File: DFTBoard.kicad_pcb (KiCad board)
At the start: 8 copper layers, 276 parts, among them CON1 AVR-JTAG-10, CON2 AVR-JTAG-10, IC1 WM8758B, IC2 IS31FL3199, IC3 CyUSB30xx-BZX, J1 JACK_TRS_5PINS, J2 JACK_TRS_5PINS, J3 JACK_TRS_5PINS, J4 JACK_TRS_5PINS, J5 GSB3211311WEU, J6 48258-0001, J7 MICRO_HDMI, Q1 IRLML2502, Q2 IRLML2502, Q3 IRLML2502, Q4 IRLML2502, Q5 IRLML2502, Q6 IRLML2502, SW1 SW_IL, U1 xc7a50tftg256, U10 NC7WZ07P6X, U11 NC7SZ125M5X, U12 GTL2002, U13 ADP198ACPZ-R7, U2 24FC128, U3 N25Q128A, U4 SC189 - 3.3V, U5 SC189 - 1.0V, U6 SC189 - 1.2V, U7 SC189 - 1.8V, U8 VL53L0X, U9 MAX3421, X1 KC5032A, Y1 19.2MHz, Y2 12MHz

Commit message: ran all FX3 BGA traces
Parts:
- added GT1: GNDTIE, DFTcustom:gndtie, F.Cu at (258.6, 129.8)
- added R94: 10k, Resistors_SMD:R_1206, F.Cu at (28.2, 37.7)
- C63: value 0.1uF -> .1uF
- C64: value 0.1uF -> 22uF
- C65: value .1uF -> .01uF; footprint Capacitors_SMD:C_0603 -> Capacitors_SMD:C_0402
- C66: value 22uF -> .1uF
- C67: value .01uF -> 0.1uF; footprint Capacitors_SMD:C_0402 -> Capacitors_SMD:C_0603
- C68: value .1uF -> 0.1uF
- R32, R73: value 100k -> 10k
- R33: value 49.9k -> 165
- R34, R43: value 50k -> 100k
- R35, R41: value 100k -> 49.9k
- R36: value 100k -> 50k
- R38, R39: value 49.9k -> 100k
- R42: value 50k -> 49.9k
- R44: value 20k -> 4.7k
- R46: value 4.7k -> 10k
- R47: value 10k -> 37.5
- R49: value 37.5 -> 50k
- R50: value 50k -> 6.04k
- R51: value 6.04k -> 200
- R52: value 200 -> 10k
- R54: value 10k -> 1k
- R55: value 1k -> 145
- R56: value 145 -> 1k
- R57: value 1k -> 90
- R58: value 90 -> 20k
- R59: value 20k -> 33; moved to B.Cu
- R61: value 33 -> 20k
- R62: value 20k -> 1k
- R64: value 1k -> 100k
- R65: value 100k -> 1k
- R66: value 1MEG -> 27k
- R67: value 1k -> 1MEG
- R68: value 27k -> 200k
- R69: value 200k -> 1k
- R70: value 1k -> 1.5k
- R72: value 1.5k -> 100k
- U3: value N25Q128A -> W25Q128FW; footprint SMD_Packages:SO-16-N -> SMD_Packages:SOIC-8-N
- moved FB2 166.0 mm to (253.2, 119.0), turned to 180 degrees
- moved C67 156.4 mm to (246.6, 126.4), turned to 180 degrees
- moved C68 150.1 mm to (249.6, 125.6), turned to 180 degrees
- moved DS1 143.0 mm to (231.8, 86.6), turned to 90 degrees
- moved CON1 130.0 mm to (111.3, 78.3)
- moved R59 109.9 mm to (259.1, 151.7), turned to 180 degrees
- moved R93 104.8 mm to (34.5, 36.6)
- moved CON2 18.5 mm to (102.2, 102.8)
- moved C64 11.0 mm to (257.9, 118.8)
- moved R61 10.0 mm to (249.3, 142.2), turned to 270 degrees
- moved C63 7.97 mm to (249.6, 119.0)
- moved IC1 7.39 mm to (82.2, 85.8)
- moved NCP1 7.21 mm to (253.9, 142.4)
- moved R60 3.64 mm to (259.1, 149.1)
- moved U9 1.73 mm to (246.5, 150.4)
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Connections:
- net Net-(C26-Pad1) renamed /Audio/MIC_IN_P
- net Net-(C26-Pad2) renamed /Audio/SFG
- net Net-(C28-Pad2) renamed /Audio/LINE_COM
- net Net-(C33-Pad1) renamed /Audio/HP_COM
- net Net-(C34-Pad1) renamed /Audio/VMID
- net Net-(C35-Pad1) renamed /Audio/MICBIAS
- net Net-(C36-Pad2) renamed /Audio/HPLOUT
- net Net-(C44-Pad1) renamed /LEDs/C_FILT
- net Net-(D1-Pad1) renamed /FPGA/Configuration/DONE_LED_D
- net Net-(D1-Pad2) renamed /FPGA/Configuration/DONE_LED_R
- net Net-(D2-Pad1) renamed /FPGA/Configuration/INIT_LED_D
- net Net-(D2-Pad2) renamed /FPGA/Configuration/INIT_LED_R
- net Net-(D3-Pad1) renamed /LEDs/LED_1R
- net Net-(D3-Pad2) renamed /LEDs/LED_1G
- net Net-(D3-Pad3) renamed /LEDs/LED_1B
- net Net-(D4-Pad1) renamed /LEDs/LED_3R
- net Net-(D4-Pad2) renamed /LEDs/LED_3G
- net Net-(D4-Pad3) renamed /LEDs/LED_3B
- net Net-(D5-Pad1) renamed /LEDs/LED_2R
- net Net-(D5-Pad2) renamed /LEDs/LED_2G
- net Net-(D5-Pad3) renamed /LEDs/LED_2B
- net Net-(D6-Pad1) renamed /SPIUSBBRIDGE/RED_LED_D
- net Net-(D7-Pad1) renamed /SPIUSBBRIDGE/BLUE_LED_D
- net Net-(DS1-Pad3) renamed /Cypress FX3/LCD_V0
- net Net-(IC1-Pad1) renamed /Audio/JACK_IN_P
- net Net-(IC1-Pad2) renamed /Audio/JACK_IN_N
- net Net-(IC1-Pad29) renamed /Audio/ROUT1
- net Net-(IC1-Pad30) renamed /Audio/LOUT1
- net Net-(IC3-PadG4) renamed /Cypress FX3/FX_P0
- net Net-(L1-Pad1) renamed /Power/3V3TOLX
- net Net-(L2-Pad1) renamed /Power/1V0TOLX
- net Net-(L3-Pad1) renamed /Power/1V2TOLX
- net Net-(L4-Pad1) renamed /Power/1V8TOLX
- net Net-(Q1-Pad1) renamed /FPGA/Configuration/DONE_LED_G
- net Net-(Q2-Pad1) renamed /FPGA/Configuration/INIT_LED_G
- net Net-(Q4-Pad1) renamed /Cypress FX3/LCD_LED_PWM
- C1 pad 2: AGND -> GND
- C10 pad 2: AGND -> GND
- C100 pad 2: AGND -> GND
- C101 pad 1: AGND -> GND
- C102 pad 1: AGND -> GND
- C103 pad 2: AGND -> GND
- C104 pad 2: AGND -> GND
- C105 pad 2: AGND -> GND
- C106 pad 1: Net-(C106-Pad1) -> /HDMI/BUF_REF
- C106 pad 2: AGND -> GND
- C107 pad 1: AGND -> GND
- C107 pad 2: /HDMI/HDMI_SHD -> HDMI_SHD
- C108 pad 2: AGND -> GND
- C109 pad 2: AGND -> GND
- C11 pad 2: AGND -> GND
- C110 pad 2: AGND -> GND
- C111 pad 2: AGND -> GND
- C112 pad 2: AGND -> GND
- C113 pad 2: AGND -> GND
- C114 pad 2: AGND -> GND
- C115 pad 2: AGND -> GND
- C116 pad 2: AGND -> GND
- C117 pad 2: AGND -> GND
- C118 pad 2: AGND -> GND
- C119 pad 2: AGND -> GND
- C12 pad 2: AGND -> GND
- C120 pad 2: AGND -> GND
- C121 pad 2: AGND -> GND
- C122 pad 2: AGND -> GND
- C123 pad 2: AGND -> GND
- C124 pad 2: AGND -> GND
- C125 pad 2: AGND -> GND
- C13 pad 2: AGND -> GND
- C14 pad 2: AGND -> GND
- C15 pad 2: AGND -> GND
- C16 pad 2: AGND -> GND
- C17 pad 2: AGND -> GND
- C18 pad 2: AGND -> GND
- C19 pad 2: AGND -> GND
- C2 pad 2: AGND -> GND
- C20 pad 2: AGND -> GND
- C21 pad 2: AGND -> GND
- C22 pad 2: AGND -> GND
- C23 pad 2: AGND -> GND
- C24 pad 2: AGND -> GND
- C25 pad 2: AGND -> GND
- C27 pad 2: AGND -> GND
- C28 pad 1: AGND -> GNDA
- C29 pad 2: AGND -> GND
- C3 pad 2: AGND -> GND
- C30 pad 2: AGND -> GND
- C31 pad 2: AGND -> GND
- C32 pad 2: AGND -> GND
- C33 pad 2: AGND -> GNDA
- C34 pad 2: AGND -> GNDA
- C35 pad 2: AGND -> GNDA
- C38 pad 2: AGND -> GND
- C39 pad 2: AGND -> GND
- C4 pad 2: AGND -> GND
- C40 pad 2: AGND -> GND
- C42 pad 2: AGND -> GND
- C43 pad 2: AGND -> GND
- C44 pad 2: AGND -> GND
- C45 pad 2: AGND -> GND
- C46 pad 2: AGND -> GND
- C47 pad 2: AGND -> GND
- C48 pad 2: AGND -> GND
- C49 pad 2: AGND -> GND
- C5 pad 2: AGND -> GND
- C50 pad 2: AGND -> GND
- C51 pad 2: AGND -> GND
- C52 pad 2: AGND -> GND
- C53 pad 2: AGND -> GND
- C54 pad 2: AGND -> GND
- C55 pad 2: AGND -> GND
- C56 pad 2: AGND -> GND
- C57 pad 2: AGND -> GND
- C58 pad 2: AGND -> GND
- C59 pad 2: AGND -> GND
- C6 pad 2: AGND -> GND
- C60 pad 2: AGND -> GND
- C61 pad 2: AGND -> GND
- C62 pad 2: AGND -> GND
- C63 pad 1: SSTX_N -> +1.2V
- C63 pad 2: /Cypress FX3/SSTXAC_N -> GND
- C64 pad 1: SSTX_P -> /Cypress FX3/U3RXVDDQ
- C64 pad 2: /Cypress FX3/SSTXAC_P -> GND
- C65 pad 1: +1.2V -> +1.8V
- C65 pad 2: AGND -> GND
- C66 pad 1: /Cypress FX3/U3RXVDDQ -> +1.2V
- C66 pad 2: AGND -> GND
- C67 pad 1: +1.8V -> SSTX_N
- C67 pad 2: AGND -> /Cypress FX3/SSTXAC_N
- C68 pad 1: +1.2V -> SSTX_P
- C68 pad 2: AGND -> /Cypress FX3/SSTXAC_P
- C69 pad 2: AGND -> GND
- C7 pad 2: AGND -> GND
- C70 pad 2: AGND -> GND
- C71 pad 2: AGND -> GND
- C72 pad 2: AGND -> GND
- C73 pad 2: AGND -> GND
- C74 pad 2: AGND -> GND
- C75 pad 2: AGND -> GND
- C76 pad 2: AGND -> GND
- C77 pad 2: AGND -> GND
- C78 pad 2: AGND -> GND
- C79 pad 2: AGND -> GND
- C8 pad 2: AGND -> GND
- C80 pad 2: AGND -> GND
- C81 pad 2: AGND -> GND
- C82 pad 2: AGND -> GND
- C83 pad 2: AGND -> GND
- C84 pad 2: AGND -> GND
- C85 pad 2: AGND -> GND
- C86 pad 2: AGND -> GND
- C87 pad 2: AGND -> GND
- C88 pad 2: AGND -> GND
- C89 pad 2: AGND -> GND
- C9 pad 2: AGND -> GND
- C90 pad 2: AGND -> GND
- C91 pad 2: AGND -> GND
- C92 pad 2: AGND -> GND
- C93 pad 2: AGND -> GND
- C94 pad 2: AGND -> GND
- C95 pad 2: AGND -> GND
- C96 pad 2: AGND -> GND
- C97 pad 2: AGND -> GND
- C98 pad 2: AGND -> GND
- C99 pad 2: AGND -> GND
- CON1 pad 10: AGND -> GND
- CON1 pad 2: AGND -> GND
- CON2 pad 10: AGND -> GND
- CON2 pad 2: AGND -> GND
- D6 pad 2: Net-(D6-Pad2) -> /SPIUSBBRIDGE/RED_LED_R
- D7 pad 2: Net-(D7-Pad2) -> /SPIUSBBRIDGE/BLUE_LED_R
- DS1 pad 1: AGND -> GND
- DS1 pad 15: Net-(DS1-Pad15) -> /Cypress FX3/LCD_LED_P
- DS1 pad 5: AGND -> GND
- IC1 pad 12: AGND -> GND
- IC1 pad 15: Net-(IC1-Pad15) -> /Audio/CSB
- IC1 pad 18: AGND -> GND
- IC1 pad 24: AGND -> GNDA
- IC1 pad 28: AGND -> GNDA
- IC1 pad 33: AGND -> GND
- IC1 pad 5: AGND -> GNDA
- IC2 pad 15: Net-(IC2-Pad15) -> /LEDs/R_EXT
- IC2 pad 16: Net-(IC2-Pad16) -> GND
- IC2 pad 7: AGND -> GND
- IC3 pad A1: AGND -> GND
- IC3 pad A8: AGND -> GND
- IC3 pad B2: AGND -> GND
- IC3 pad B4: AGND -> GND
- IC3 pad B7: AGND -> GND
- IC3 pad B8: AGND -> GND
- IC3 pad B9: AGND -> GND
- IC3 pad D8: AGND -> GND
- IC3 pad E2: AGND -> GND
- IC3 pad E6: AGND -> GND
- IC3 pad G1: AGND -> GND
- IC3 pad G11: AGND -> GND
- IC3 pad H4: Net-(IC3-PadH4) -> /Cypress FX3/FX_P1
- IC3 pad K3: AGND -> GND
- IC3 pad K4: AGND -> GND
- IC3 pad L1: AGND -> GND
- IC3 pad L11: AGND -> GND
- IC3 pad L2: AGND -> GND
- IC3 pad L3: AGND -> GND
- IC3 pad L6: AGND -> GND
- J1 pad S: AGND -> GNDA
- J1 pad TB: Net-(J1-PadTB) -> /Audio/INSWITCH
- J2 pad RB: Net-(J2-PadRB) -> /Audio/HPSWITCH
- J2 pad S: AGND -> GNDA
- J3 pad R: AGND -> GNDA
- J3 pad RB: AGND -> GNDA
- J3 pad S: AGND -> GNDA
- J3 pad TB: Net-(J3-PadTB) -> /Audio/RSWITCH
- J4 pad R: AGND -> GNDA
- J4 pad RB: AGND -> GNDA
- J4 pad S: AGND -> GNDA
- J4 pad TB: Net-(J4-PadTB) -> /Audio/LSWITCH
- J5 pad 4: AGND -> GNDPWR
- J5 pad 7: AGND -> GNDPWR
- J6 pad 4: AGND -> GND
- J6 pad P1: AGND -> GND
- J6 pad P2: AGND -> GND
- J7 pad 1: Net-(J7-Pad1) -> /HDMI/HDMI_DETECT_PIN
- J7 pad 10: AGND -> GND
- J7 pad 13: AGND -> GND
- J7 pad 16: AGND -> GND
- J7 pad 17: Net-(J7-Pad17) -> HDMI_SCL_B
- J7 pad 18: Net-(J7-Pad18) -> HDMI_SDA_B
- J7 pad 4: AGND -> GND
- J7 pad 7: AGND -> GND
- J7 pad SHD: /HDMI/HDMI_SHD -> HDMI_SHD
- JP1 pad 2: Net-(IC3-PadH4) -> /Cypress FX3/FX_P1
- MIC1 pad 2: AGND -> GNDA
- MIC1 pad 3: AGND -> GNDA
- NCP1 pad 2: AGND -> GND
- NCP1 pad 3: AGND -> GND
- Q1 pad 2: AGND -> GND
- Q2 pad 2: AGND -> GND
- Q3 pad 2: AGND -> GND
- Q4 pad 2: AGND -> GND
- Q5 pad 1: Net-(Q5-Pad1) -> /SPIUSBBRIDGE/RED_LED_G
- Q5 pad 2: AGND -> GND
- Q6 pad 1: Net-(Q6-Pad1) -> /SPIUSBBRIDGE/BLUE_LED_G
- Q6 pad 2: AGND -> GND
- R32 pad 2: Net-(J1-PadTB) -> TEMPO_SW
- R33 pad 1: JD_IN -> +5V
- R33 pad 2: Net-(J1-PadTB) -> /FPGA/GPIF II/TEMPO_LED_R
- R34 pad 2: Net-(IC1-Pad15) -> /Audio/INSWITCH
- R35 pad 1: Net-(J3-PadTB) -> JD_IN
- R35 pad 2: +3V3 -> /Audio/INSWITCH
- R36 pad 1: Net-(J4-PadTB) -> +1.8V
- R36 pad 2: +3V3 -> /Audio/CSB
- R37 pad 1: Net-(J2-PadRB) -> /Audio/RSWITCH
- R38 pad 1: JD_ROUT -> /Audio/LSWITCH
- R38 pad 2: Net-(J3-PadTB) -> +3V3
- R39 pad 1: JD_LOUT -> /Audio/HPSWITCH
- R39 pad 2: Net-(J4-PadTB) -> +3V3
- R40 pad 1: JD_HOUT -> JD_ROUT
- R40 pad 2: Net-(J2-PadRB) -> /Audio/RSWITCH
- R41 pad 1: Net-(IC2-Pad15) -> JD_LOUT
- R41 pad 2: AGND -> /Audio/LSWITCH
- R42 pad 1: Net-(IC2-Pad16) -> JD_HOUT
- R42 pad 2: AGND -> /Audio/HPSWITCH
- R43 pad 1: Net-(R43-Pad1) -> /LEDs/R_EXT
- R43 pad 2: +1.8V -> GND
- R44 pad 1: +1.8V -> I2C_SCLK
- R44 pad 2: Net-(R44-Pad2) -> +1.8V
- R45 pad 1: I2C_SCLK -> I2C_SDIN
- R46 pad 1: I2C_SDIN -> +1.8V
- R46 pad 2: +1.8V -> /Cypress FX3/FX_P1
- R47 pad 1: +1.8V -> /Cypress FX3/LCD_LED_P
- R47 pad 2: Net-(IC3-PadH4) -> +5V
- R49 pad 1: Net-(DS1-Pad15) -> CVDDQ
- R49 pad 2: +5V -> /Cypress FX3/nRESET
- R50 pad 1: CVDDQ -> /Cypress FX3/RUSB2
- R50 pad 2: /Cypress FX3/nRESET -> GND
- R51 pad 1: /Cypress FX3/RUSB2 -> /Cypress FX3/RUSB3
- R51 pad 2: AGND -> GND
- R52 pad 1: /Cypress FX3/RUSB3 -> +1.8V
- R52 pad 2: AGND -> RF_SD
- R53 pad 2: RF_SD -> RF_IRQ
- R54 pad 1: +1.8V -> /SPIUSBBRIDGE/RED_LED_G
- R54 pad 2: RF_IRQ -> /SPIUSBBRIDGE/GPOUT5_RED_LED
- R55 pad 1: Net-(Q5-Pad1) -> /SPIUSBBRIDGE/RED_LED_R
- R55 pad 2: Net-(R55-Pad2) -> +5V
- R56 pad 1: Net-(D6-Pad2) -> /SPIUSBBRIDGE/BLUE_LED_G
- R56 pad 2: +5V -> /SPIUSBBRIDGE/GPOUT6_BLUE_LED
- R57 pad 1: Net-(Q6-Pad1) -> /SPIUSBBRIDGE/BLUE_LED_R
- R57 pad 2: Net-(R57-Pad2) -> +5V
- R58 pad 1: Net-(D7-Pad2) -> +1.8V
- R58 pad 2: +5V -> /SPIUSBBRIDGE/RES
- R59 pad 1: +1.8V -> SPIUSB_D_P
- R59 pad 2: Net-(R59-Pad2) -> /SPIUSBBRIDGE/SPIUSB_DT_P
- R60 pad 1: SPIUSB_D_P -> SPIUSB_D_N
- R60 pad 2: /SPIUSBBRIDGE/SPIUSB_DT_P -> /SPIUSBBRIDGE/SPIUSB_DT_N
- R61 pad 1: SPIUSB_D_N -> +5V
- R61 pad 2: /SPIUSBBRIDGE/SPIUSB_DT_N -> USB_FAULT
- R62 pad 1: +5V -> +3V3
- R62 pad 2: USB_FAULT -> HDMI_SCL
- R63 pad 2: HDMI_SCL -> HDMI_SDA
- R64 pad 1: +3V3 -> /HDMI/HDMI_DETECT_PIN
- R64 pad 2: HDMI_SDA -> GND
- R65 pad 1: Net-(J7-Pad1) -> /HDMI/HDMI_DETECT_B2
- R65 pad 2: AGND -> /HDMI/HDMI_DETECT_PIN
- R66 pad 1: AGND -> (no net)
- R66 pad 2: /HDMI/HDMI_SHD -> +3V3
- R67 pad 1: Net-(R67-Pad1) -> GND
- R67 pad 2: Net-(J7-Pad1) -> HDMI_SHD
- R68 pad 1: (no net) -> HDMI_5V0
- R68 pad 2: +3V3 -> /HDMI/BUF_REF
- R69 pad 1: HDMI_5V0 -> HDMI_DETECT
- R69 pad 2: Net-(C106-Pad1) -> /HDMI/HDMI_DETECT_B1
- R70 pad 1: HDMI_DETECT -> HDMI_5V0
- R70 pad 2: Net-(R70-Pad2) -> HDMI_SCL_B
- R71 pad 2: Net-(J7-Pad17) -> HDMI_SDA_B
- R72 pad 1: HDMI_5V0 -> HDMI_DETECT
- R72 pad 2: Net-(J7-Pad18) -> GND
- R73 pad 1: HDMI_DETECT -> +1.8V
- R73 pad 2: AGND -> ENCC0_SW
- R74 pad 2: ENCC0_SW -> ENCC2_SW
- R75 pad 2: ENCC2_SW -> Net-(R75-Pad2)
- R79 pad 1: +1.8V -> ENCC0_Q0
- R79 pad 2: Net-(R79-Pad2) -> Net-(R75-Pad2)
- R80 pad 1: ENCC0_Q0 -> ENCC0_Q1
- R80 pad 2: Net-(R76-Pad2) -> Net-(R77-Pad2)
- R81 pad 1: ENCC0_Q1 -> ENCC2_Q0
- R81 pad 2: Net-(R78-Pad2) -> Net-(R76-Pad2)
- R82 pad 1: ENCC2_Q0 -> ENCC2_Q1
- R82 pad 2: Net-(R77-Pad2) -> Net-(R78-Pad2)
- R83 pad 1: ENCC2_Q1 -> +1.8V
- R83 pad 2: Net-(R79-Pad2) -> ENCC1_SW
- R84 pad 1: +1.8V -> +3V3
- R84 pad 2: ENCC1_SW -> ENCC3_SW
- R85 pad 1: +3V3 -> +1.8V
- R85 pad 2: ENCC3_SW -> Net-(R85-Pad2)
- R86 pad 1: +1.8V -> +3V3
- R87 pad 1: +3V3 -> +1.8V
- R88 pad 1: +1.8V -> +3V3
- R89 pad 1: +3V3 -> ENCC1_Q0
- R89 pad 2: Net-(R89-Pad2) -> Net-(R85-Pad2)
- R90 pad 1: ENCC1_Q0 -> ENCC1_Q1
- R90 pad 2: Net-(R86-Pad2) -> Net-(R87-Pad2)
- R91 pad 1: ENCC1_Q1 -> ENCC3_Q0
- R91 pad 2: Net-(R88-Pad2) -> Net-(R86-Pad2)
- R92 pad 1: ENCC3_Q0 -> ENCC3_Q1
- R92 pad 2: Net-(R87-Pad2) -> Net-(R88-Pad2)
- R93 pad 1: ENCC3_Q1 -> +1.8V
- R93 pad 2: Net-(R89-Pad2) -> Net-(R93-Pad2)
- ROT1 pad A: Net-(R76-Pad2) -> Net-(R75-Pad2)
- ROT1 pad B: Net-(R78-Pad2) -> Net-(R77-Pad2)
- ROT1 pad C: AGND -> GND
- ROT1 pad S2: AGND -> GND
- ROT2 pad A: Net-(R77-Pad2) -> Net-(R76-Pad2)
- ROT2 pad B: Net-(R79-Pad2) -> Net-(R78-Pad2)
- ROT2 pad C: AGND -> GND
- ROT2 pad S2: AGND -> GND
- ROT3 pad A: Net-(R86-Pad2) -> Net-(R85-Pad2)
- ROT3 pad B: Net-(R88-Pad2) -> Net-(R87-Pad2)
- ROT3 pad C: AGND -> GND
- ROT3 pad S2: AGND -> GND
- ROT4 pad A: Net-(R87-Pad2) -> Net-(R86-Pad2)
- ROT4 pad B: Net-(R89-Pad2) -> Net-(R88-Pad2)
- ROT4 pad C: AGND -> GND
- ROT4 pad S2: AGND -> GND
- RV1 pad 1: AGND -> GND
- SW1 pad 1: AGND -> GND
- SW1 pad 4: +5V -> /FPGA/GPIF II/TEMPO_LED_R
- U1 pad A1: AGND -> GND
- U1 pad A11: AGND -> GND
- U1 pad A16: AGND -> GND
- U1 pad B13: AGND -> GND
- U1 pad B8: AGND -> GND
- U1 pad C10: AGND -> GND
- U1 pad C15: AGND -> GND
- U1 pad C5: AGND -> GND
- U1 pad D12: AGND -> GND
- U1 pad D2: AGND -> GND
- U1 pad E14: AGND -> GND
- U1 pad E7: AGND -> GND
- U1 pad E9: AGND -> GND
- U1 pad F10: AGND -> GND
- U1 pad F16: AGND -> GND
- U1 pad F6: AGND -> GND
- U1 pad F8: AGND -> GND
- U1 pad G13: AGND -> GND
- U1 pad G3: AGND -> GND
- U1 pad G7: AGND -> GND
- U1 pad G9: AGND -> GND
- U1 pad H15: AGND -> GND
- U1 pad H6: AGND -> GND
- U1 pad H7: AGND -> GND
- U1 pad H8: AGND -> GND
- U1 pad J11: AGND -> GND
- U1 pad J12: AGND -> GND
- U1 pad J7: AGND -> GND
- U1 pad J8: AGND -> GND
- U1 pad J9: AGND -> GND
- U1 pad K14: AGND -> GND
- U1 pad K4: AGND -> GND
- U1 pad K6: AGND -> GND
- U1 pad K7: AGND -> GND
- U1 pad K8: AGND -> GND
- U1 pad L1: AGND -> GND
- U1 pad L11: AGND -> GND
- U1 pad M3: AGND -> GND
- U1 pad M8: AGND -> GND
- U1 pad N15: AGND -> GND
- U1 pad N5: AGND -> GND
- U1 pad P12: AGND -> GND
- U1 pad P2: AGND -> GND
- U1 pad R4: AGND -> GND
- U1 pad R9: AGND -> GND
- U1 pad T1: AGND -> GND
- U1 pad T16: AGND -> GND
- U1 pad T6: AGND -> GND
- U10 pad 1: Net-(J7-Pad1) -> /HDMI/HDMI_DETECT_PIN
- U10 pad 2: AGND -> GND
- U10 pad 6: Net-(R70-Pad2) -> /HDMI/HDMI_DETECT_B1
- U11 pad 3: AGND -> GND
- U11 pad 4: Net-(R67-Pad1) -> /HDMI/HDMI_DETECT_B2
- U12 pad 1: AGND -> GND
- U12 pad 5: Net-(J7-Pad18) -> HDMI_SDA_B
- U12 pad 6: Net-(J7-Pad17) -> HDMI_SCL_B
- U12 pad 7: Net-(C106-Pad1) -> /HDMI/BUF_REF
- U12 pad 8: Net-(C106-Pad1) -> /HDMI/BUF_REF
- U13 pad 3: AGND -> GND
- U13 pad 4: AGND -> GND
- U13 pad P: AGND -> GND
- U2 pad 1: AGND -> GND
- U2 pad 2: AGND -> GND
- U2 pad 3: AGND -> GND
- U2 pad 4: AGND -> GND
- U3 pad 1: Net-(R43-Pad1) -> SPIMEM_SS
- U3 pad 2: +1.8V -> SPI_MISO
- U3 pad 3: (no net) -> Net-(R93-Pad2)
- U3 pad 4: (no net) -> GND
- U3 pad 5: (no net) -> SPI_MOSI
- U3 pad 6: (no net) -> SPI_CLK
- U3 pad 7: SPIMEM_SS -> Net-(R94-Pad2)
- U3 pad 8: SPI_MISO -> +1.8V
- U4 pad 2: AGND -> GND
- U5 pad 2: AGND -> GND
- U6 pad 2: AGND -> GND
- U7 pad 2: AGND -> GND
- U8 pad 12: AGND -> GND
- U8 pad 2: AGND -> GND
- U8 pad 3: AGND -> GND
- U8 pad 4: AGND -> GND
- U8 pad 6: AGND -> GND
- U9 pad 10: Net-(R57-Pad2) -> /SPIUSBBRIDGE/GPOUT6_BLUE_LED
- U9 pad 12: Net-(R59-Pad2) -> /SPIUSBBRIDGE/RES
- U9 pad 19: AGND -> GND
- U9 pad 3: AGND -> GND
- U9 pad 9: Net-(R55-Pad2) -> /SPIUSBBRIDGE/GPOUT5_RED_LED
- X1 pad 2: AGND -> GND
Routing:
- net GND: track 0.00 -> 45.7 mm, vias 0 -> 65
- net LCD_E: track 0.00 -> 41.0 mm, vias 0 -> 1
- net AGND: track 40.6 -> 0.00 mm, vias 61 -> 0
- net SPI_CLK: track 0.00 -> 19.5 mm, vias 0 -> 1
- net PWM_LCD_DIM: track 0.00 -> 15.0 mm, vias 0 -> 1
- net USB_FAULT: track 0.00 -> 14.2 mm, vias 0 -> 1
- net SPIUSB_INT: track 0.00 -> 12.7 mm, vias 0 -> 1
- net RF_IRQ: track 0.00 -> 11.1 mm, vias 0 -> 1
- net /Cypress FX3/U3RXVDDQ: track 0.00 -> 10.8 mm
- net LCD_RS: track 0.00 -> 10.7 mm, vias 0 -> 1
- net SPIUSB_SS: track 0.00 -> 10.7 mm, vias 0 -> 1
- net LCD_D5: track 0.00 -> 10.3 mm, vias 0 -> 1
- net I2S_DACSD: track 0.00 -> 10.2 mm
- net /Cypress FX3/nRESET: track 0.00 -> 10.0 mm, vias 0 -> 1
- net /Cypress FX3/RUSB3: track 0.00 -> 9.59 mm, vias 0 -> 1
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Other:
- net class Crystal added: clearance 0.08, trace_width 0.15, via_dia 0.48, via_drill 0.25
- net class LEDs added: clearance 0.08, trace_width 0.15, via_dia 0.48, via_drill 0.25
- net class Main Power added: clearance 0.08, trace_width 0.6, via_dia 0.48, via_drill 0.25

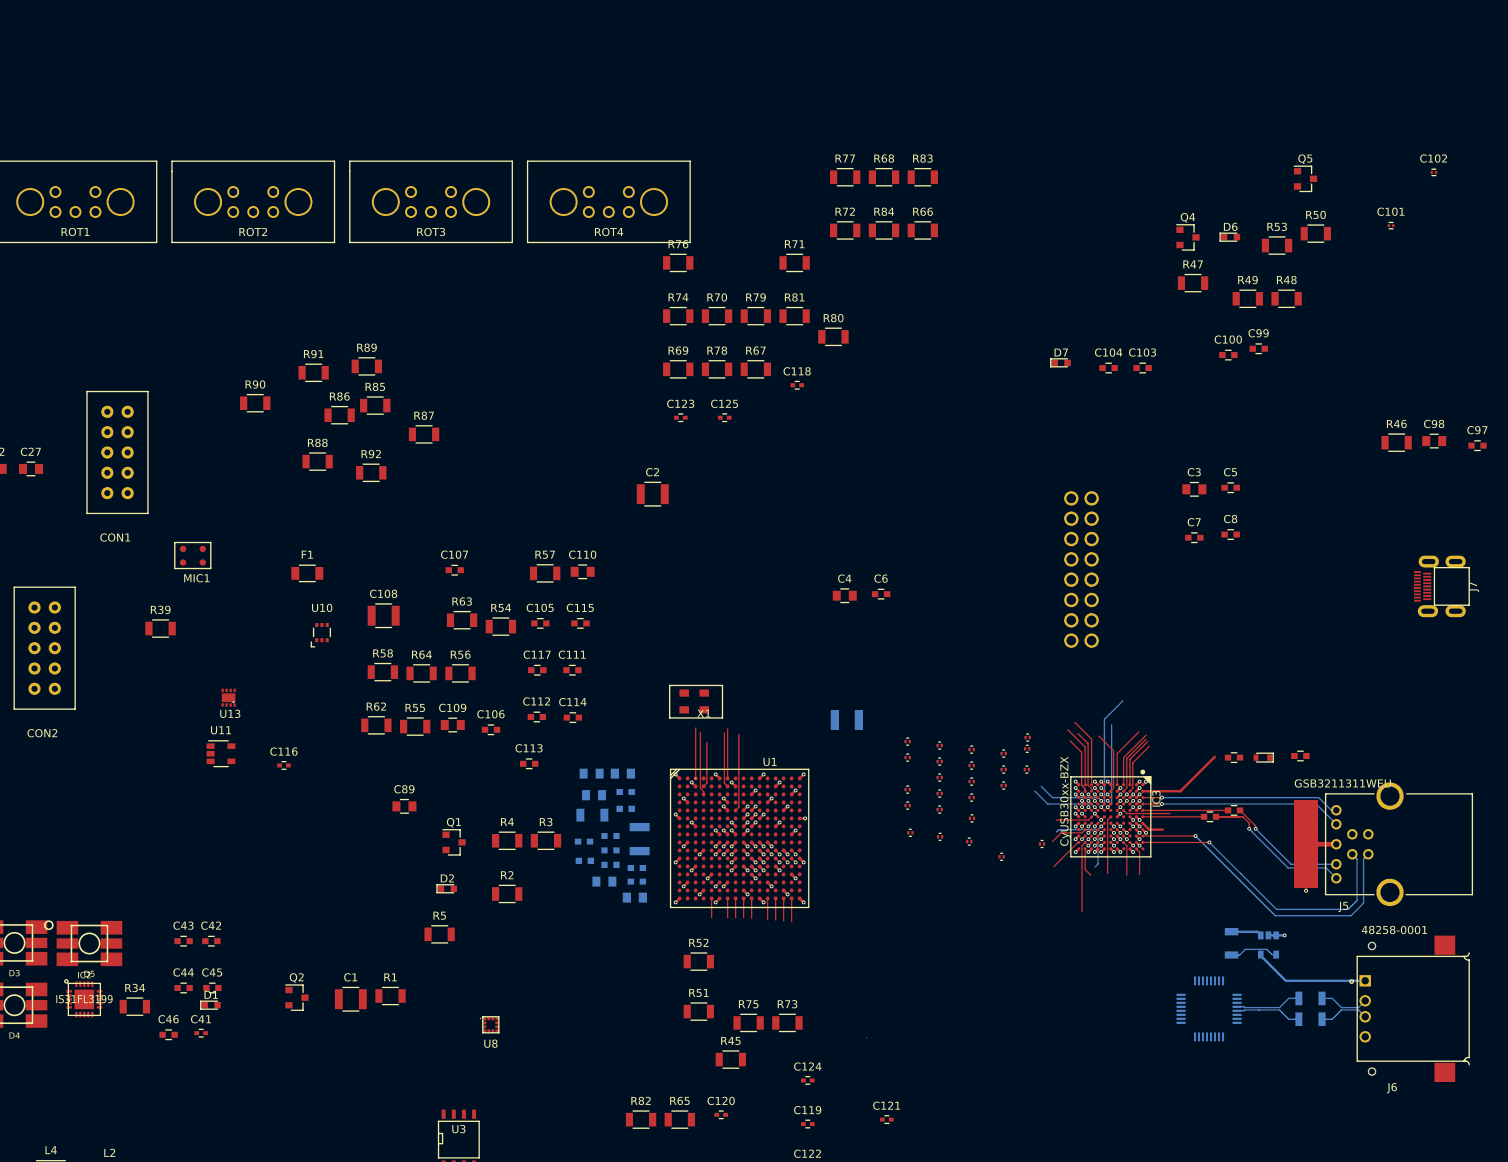
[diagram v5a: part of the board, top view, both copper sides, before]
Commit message: started adding jack
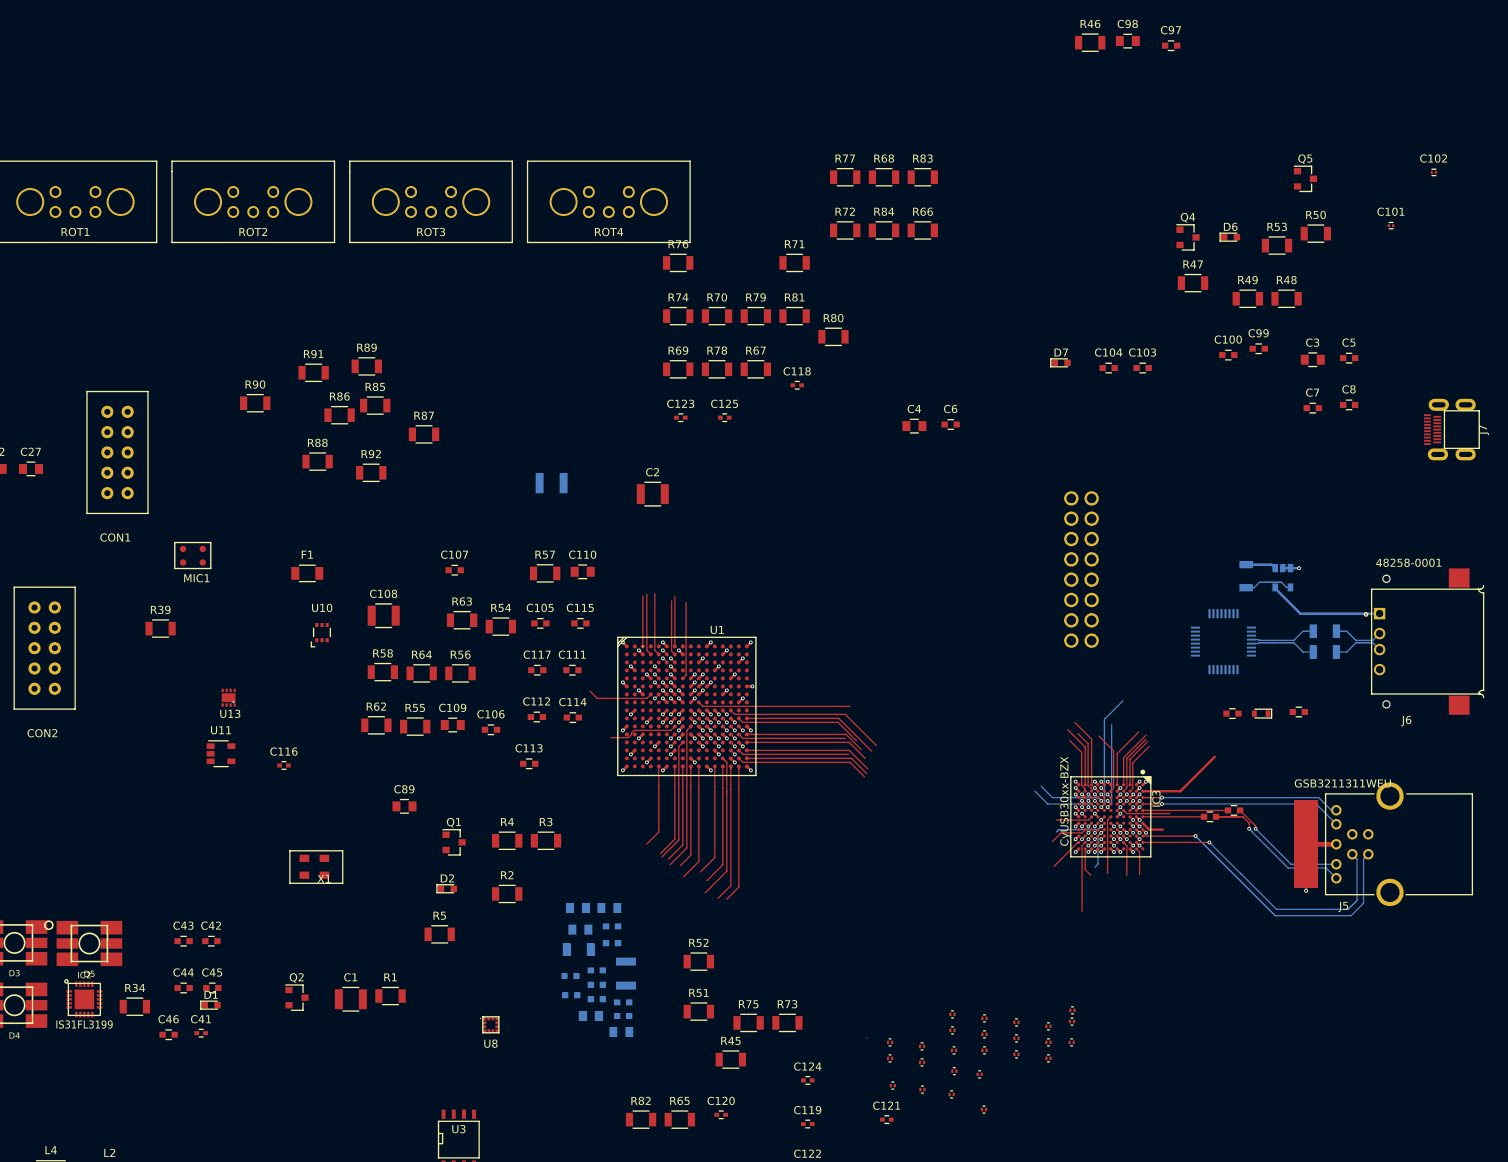
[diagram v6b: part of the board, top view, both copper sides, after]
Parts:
- moved C97 63.0 mm to (241.7, 30.0)
- moved R46 63.0 mm to (231.6, 29.6)
- moved C98 63.0 mm to (236.3, 29.4)
- moved X1 51.8 mm to (135.9, 133.7)
- moved C25 47.3 mm to (164.3, 84.7)
- moved J6 45.9 mm to (273.8, 104.5)
- moved NCP1 45.9 mm to (255.7, 96.5)
- moved U9 45.9 mm to (248.3, 104.5)
- moved R59 45.9 mm to (260.9, 105.8)
- moved R60 45.9 mm to (260.9, 103.2)
- moved R61 45.9 mm to (251.1, 96.3)
- moved R10 34.6 mm to (226.4, 152.6)
- moved R11 34.6 mm to (226.4, 154.6)
- moved R14 34.6 mm to (229.3, 154.6)
- moved R15 34.6 mm to (222.4, 152.1)
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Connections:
- U1 pad N13: (no net) -> GPIF_SLRD#T
- U1 pad P13: (no net) -> GPIF_PKTEND#T
- U1 pad P6: GPIF_PKTEND#T -> (no net)
- U1 pad T7: GPIF_SLRD#T -> (no net)
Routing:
- net LCD_E: track 41.0 -> 12.6 mm
- net GPIF_FLAGAT: track 0.00 -> 23.0 mm, vias 0 -> 1
- net GPIF_FLAGBT: track 0.00 -> 20.0 mm
- net CONFIG_DONE: track 6.43 -> 25.5 mm
- net CONFIG_PROGRAM: track 0.00 -> 18.4 mm
- net TEMPO_SW: track 0.11 -> 18.2 mm
- net GD_7T: track 0.00 -> 17.4 mm, vias 0 -> 1
- net GD_11T: track 0.00 -> 17.3 mm
- net AX_TMS: track 0.00 -> 17.1 mm, vias 0 -> 1
- net GD_9T: track 0.71 -> 17.7 mm
- net GD_10T: track 0.71 -> 17.6 mm
- net I2S_MCLK: track 8.45 -> 25.3 mm, vias 1 -> 2
- net GD_2T: track 0.00 -> 16.7 mm
- net AX_TDI: track 0.00 -> 16.1 mm, vias 0 -> 1
- net GD_4T: track 0.00 -> 16.1 mm
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
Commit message: more moving around components and connecting. all cypress and FPGA bypass caps placed
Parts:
- added C126: 10uF, Capacitors_SMD:C_0805, F.Cu at (26.1, 46.8)
- added C127: .1uF, Capacitors_SMD:C_0603, F.Cu at (29.1, 51.8)
- added C128: .1uF, Capacitors_SMD:C_0603, F.Cu at (26.4, 56.3)
- added C129: 10uF, Capacitors_SMD:C_0805, F.Cu at (38.3, 45.9)
- added C130: .1uF, Capacitors_SMD:C_0603, F.Cu at (33.1, 58.1)
- added C131: .1uF, Capacitors_SMD:C_0603, F.Cu at (38.5, 53.5)
- added C132: .1uF, Capacitors_SMD:C_0603, F.Cu at (38.0, 59.4)
- added C133: .1uF, Capacitors_SMD:C_0603, F.Cu at (31.9, 43.5)
- added C134: 15pF, Capacitors_SMD:C_0402, F.Cu at (42.2, 50.6)
- added C135: 15pF, Capacitors_SMD:C_0402, F.Cu at (32.6, 49.9)
- added C136: 47uF, Capacitors_SMD:C_1210, F.Cu at (147.5, 165.1)
- added C137, C138: 4.7uF, Capacitors_SMD:C_0805, F.Cu at (147.5, 165.1)
- added C139, C140, C141, C142: .47uF, Capacitors_SMD:C_0603, F.Cu at (147.5, 165.1)
- added C36: 220uF, Capacitors_ThroughHole:CP_Radial_D6.3mm_P2.50mm, F.Cu at (69.9, 15.6)
- added C37: 220uF, Capacitors_ThroughHole:CP_Radial_D6.3mm_P2.50mm, F.Cu at (99.9, 33.8)
- added D10: LED RED, LEDs:LED_0603, F.Cu at (283.7, 84.5)
- added D11: LED BLUE, LEDs:LED_0603, F.Cu at (283.5, 79.8)
- added D12: BAS16XV2T1G, Diodes_SMD:D_SOD-523, F.Cu at (80.7, 65.7)
- added J8: GSB3211311WEU, GSB3211311WEU:AMPHENOL_GSB3211311WEU, B.Cu at (25.0, 145.0)
- added J9: 48258-0001, 48258-0001:MOLEX_48258-0001, F.Cu at (273.6, 122.8)
- added JP2: POWERJUMPER, DFTcustom:JUMPER_2PIN, F.Cu at (283.7, 84.8)
- added NCP2: NCP361, DFTcustom:TSOP-5, F.Cu at (52.8, 35.8)
- added R100: 10k, Resistors_SMD:R_1206, F.Cu at (283.7, 85.4)
- added R101: 649, Resistors_SMD:R_1206, F.Cu at (283.7, 85.5)
- added R102: 20k, Resistors_SMD:R_1206, F.Cu at (283.7, 85.1)
- added R95: 10k, Resistors_SMD:R_1206, F.Cu at (278.2, 109.4)
- added R96: 10k, Resistors_SMD:R_1206, F.Cu at (283.6, 91.7)
- added R97: 10k, Resistors_SMD:R_1206, F.Cu at (283.7, 84.9)
- added R98: 10k, Resistors_SMD:R_1206, F.Cu at (283.7, 85.2)
- added R99: 10k, Resistors_SMD:R_1206, F.Cu at (283.7, 85.0)
- added U14: W9751G6KB, DFTcustom:WBGA-84, F.Cu at (221.1, 111.2)
- added U15: CY7C65634-28LTXC, Housings_DFN_QFN:QFN-28-1EP_5x5mm_Pitch0.5mm, B.Cu at (251.3, 104.6)
- added Y3: ECS-120-20-3X-TR, DFTcustom:ABLS-12.000MHZ, F.Cu at (121.4, 23.6)
- C1, C108, C109, C110, C111, C112, C113, C114, C2, C3, C4, C5, C53, C54, C55, C56, C57, C58, C59, C6, C60, C61, C62, C63, C64, C65, C66, C69, C7, C70, C71, C72, C73, C74, C75, C76, C77, C78, C79, C8, C80, C81, C82, C83, C84, C85, C86, C87, C88, J1, J2, J3, J4, J5: moved to B.Cu
- D6: value LED RED -> DB2W40100L; footprint LEDs:LED_0603 -> DFTcustom:DB2W40100L
- D7: value LED BLUE -> DB2W40100L; footprint LEDs:LED_0603 -> DFTcustom:DB2W40100L
- R44, R45: value 4.7k -> 10k
- R46: value 10k -> 4.7k
- R47: value 37.5 -> 4.7k
- R48, R54, R56: value 1k -> 10k
- R49: value 50k -> 37.5
- R50: value 6.04k -> 1k
- R51: value 200 -> 50k
- R52: value 10k -> 6.04k
- R53: value 10k -> 200
- R55: value 145 -> 10k
- R57: value 90 -> 10k
- R58: value 20k -> 10k
- R59: value 33 -> 10k; moved to F.Cu
- R60: value 33 -> 1k; moved to F.Cu
- R61: value 20k -> 145
- R63: value 1k -> 90
- R64: value 100k -> 20k
- R65: value 1k -> 33
- R66: value 27k -> 33
- R67: value 1MEG -> 20k
- R68: value 200k -> 1k
- R70: value 1.5k -> 100k
- R71: value 1.5k -> 1k
- R72: value 100k -> 27k
- R73: value 10k -> 1MEG
- R74: value 10k -> 200k
- R75: value 10k -> 1k
- R76, R77: value 10k -> 1.5k
- R78: value 10k -> 100k
- U9: moved to F.Cu
- Y2: value 12MHz -> ECS-120-20-3X-TR
- moved C83 185.5 mm to (241.8, 130.2), turned to 270 degrees
- moved C73 174.9 mm to (232.6, 128.6)
- moved C70 172.6 mm to (226.8, 131.2), turned to 90 degrees
- moved C75 172.5 mm to (238.6, 143.6)
- moved C72 171.0 mm to (234.6, 132.4), turned to 90 degrees
- moved C80 170.8 mm to (235.0, 128.6)
- moved C61 159.6 mm to (234.6, 130.2)
- moved C84 157.9 mm to (232.6, 136.8)
- moved C87 157.7 mm to (226.0, 143.6)
- moved C85 156.9 mm to (229.0, 143.8)
- moved C54 156.7 mm to (226.8, 134.3), turned to 270 degrees
- moved C79 156.6 mm to (225.8, 128.8)
- moved C59 155.2 mm to (233.8, 141.2), turned to 90 degrees
- moved C58 152.7 mm to (228.0, 137.7), turned to 270 degrees
- moved C78 152.0 mm to (235.0, 136.8)
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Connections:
- net Net-(C101-Pad2) renamed /SPIUSBBRIDGE/SPIUSB_XO
- net Net-(C102-Pad2) renamed /SPIUSBBRIDGE/SPIUSB_XI
- net SPIUSB_VBUS renamed SPIUSB_VBUS1
- C35 pad 1: /Audio/MICBIAS -> MICBIAS
- D6 pad 1: /SPIUSBBRIDGE/RED_LED_D -> ORPOWER
- D6 pad 2: /SPIUSBBRIDGE/RED_LED_R -> USB_5V
- D7 pad 1: /SPIUSBBRIDGE/BLUE_LED_D -> ORPOWER
- D7 pad 2: /SPIUSBBRIDGE/BLUE_LED_R -> JACK_5V
- IC1 pad 23: (no net) -> /Audio/HPROUT_CAP
- IC1 pad 25: (no net) -> /Audio/HPLOUT_CAP
- IC1 pad 32: /Audio/MICBIAS -> MICBIAS
- IC3 pad E10: (no net) -> Net-(IC3-PadE10)
- IC3 pad H6: USB_FAULT -> (no net)
- J2 pad R: (no net) -> /Audio/HPROUT
- J5 pad 1: +5V -> USB_5V
- J5 pad 5: SSTX_N -> SSTX_P
- J5 pad 6: SSTX_P -> SSTX_N
- J5 pad 8: SSRX_P -> SSRX_N
- J5 pad 9: SSRX_N -> SSRX_P
- J6 pad 2: SPIUSB_D_N -> SPIUSB1_D_N
- J6 pad 3: SPIUSB_D_P -> SPIUSB1_D_P
- MIC1 pad 1: +3V3 -> MICBIAS
- NCP1 pad 4: USB_FAULT -> SPIUSB_FAULT1
- Q3 pad 3: (no net) -> /FPGA/GPIF II/TEMPO_LED_D
- R44 pad 1: I2C_SCLK -> +1.8V
- R44 pad 2: +1.8V -> Net-(R44-Pad2)
- R45 pad 1: I2C_SDIN -> +1.8V
- R45 pad 2: +1.8V -> Net-(R45-Pad2)
- R46 pad 1: +1.8V -> I2C_SCLK
- R46 pad 2: /Cypress FX3/FX_P1 -> +1.8V
- R47 pad 1: /Cypress FX3/LCD_LED_P -> I2C_SDIN
- R47 pad 2: +5V -> +1.8V
- R48 pad 1: /Cypress FX3/LCD_LED_PWM -> +1.8V
- R48 pad 2: PWM_LCD_DIM -> /Cypress FX3/FX_P1
- R49 pad 1: CVDDQ -> /Cypress FX3/LCD_LED_P
- R49 pad 2: /Cypress FX3/nRESET -> +5V
- R50 pad 1: /Cypress FX3/RUSB2 -> /Cypress FX3/LCD_LED_PWM
- R50 pad 2: GND -> PWM_LCD_DIM
- R51 pad 1: /Cypress FX3/RUSB3 -> CVDDQ
- R51 pad 2: GND -> /Cypress FX3/nRESET
- R52 pad 1: +1.8V -> /Cypress FX3/RUSB2
- R52 pad 2: RF_SD -> GND
- R53 pad 1: +1.8V -> /Cypress FX3/RUSB3
- R53 pad 2: RF_IRQ -> GND
- R54 pad 1: /SPIUSBBRIDGE/RED_LED_G -> GND
- R54 pad 2: /SPIUSBBRIDGE/GPOUT5_RED_LED -> ORPOWER
- R55 pad 1: /SPIUSBBRIDGE/RED_LED_R -> GND
- R55 pad 2: +5V -> JACK_5V
- R56 pad 1: /SPIUSBBRIDGE/BLUE_LED_G -> +1.8V
- R56 pad 2: /SPIUSBBRIDGE/GPOUT6_BLUE_LED -> Net-(C127-Pad2)
- R57 pad 1: /SPIUSBBRIDGE/BLUE_LED_R -> Net-(C127-Pad2)
- R57 pad 2: +5V -> GND
- R58 pad 2: /SPIUSBBRIDGE/RES -> RF_SD
- R59 pad 1: SPIUSB_D_P -> +1.8V
- R59 pad 2: /SPIUSBBRIDGE/SPIUSB_DT_P -> RF_IRQ
- R60 pad 1: SPIUSB_D_N -> /SPIUSBBRIDGE/RED_LED_G
- R60 pad 2: /SPIUSBBRIDGE/SPIUSB_DT_N -> STATLED_RED
- R61 pad 1: +5V -> /SPIUSBBRIDGE/RED_LED_R
- R61 pad 2: USB_FAULT -> +5V
- R62 pad 1: +3V3 -> /SPIUSBBRIDGE/BLUE_LED_G
- R62 pad 2: HDMI_SCL -> STATLED_BLUE
- R63 pad 1: +3V3 -> /SPIUSBBRIDGE/BLUE_LED_R
- R63 pad 2: HDMI_SDA -> +5V
- R64 pad 1: /HDMI/HDMI_DETECT_PIN -> /SPIUSBBRIDGE/RES
- R64 pad 2: GND -> +1.8V
- R65 pad 1: /HDMI/HDMI_DETECT_B2 -> SPIUSB_D_P
- R65 pad 2: /HDMI/HDMI_DETECT_PIN -> /SPIUSBBRIDGE/SPIUSB_DT_P
- R66 pad 1: (no net) -> SPIUSB_D_N
- R66 pad 2: +3V3 -> /SPIUSBBRIDGE/SPIUSB_DT_N
- R67 pad 1: GND -> +5V
- R67 pad 2: HDMI_SHD -> SPIUSB_FAULT1
- R68 pad 1: HDMI_5V0 -> +3V3
- R68 pad 2: /HDMI/BUF_REF -> HDMI_SCL
- R69 pad 1: HDMI_DETECT -> +3V3
- R69 pad 2: /HDMI/HDMI_DETECT_B1 -> HDMI_SDA
- R70 pad 1: HDMI_5V0 -> /HDMI/HDMI_DETECT_PIN
- R70 pad 2: HDMI_SCL_B -> GND
- R71 pad 1: HDMI_5V0 -> /HDMI/HDMI_DETECT_B2
- R71 pad 2: HDMI_SDA_B -> /HDMI/HDMI_DETECT_PIN
- R72 pad 1: HDMI_DETECT -> Net-(D12-Pad2)
- R72 pad 2: GND -> +3V3
- R73 pad 1: +1.8V -> GND
- R73 pad 2: ENCC0_SW -> HDMI_SHD
- R74 pad 1: +1.8V -> HDMI_5V0
- R74 pad 2: ENCC2_SW -> /HDMI/BUF_REF
- R75 pad 1: +1.8V -> HDMI_DETECT
- R75 pad 2: Net-(R75-Pad2) -> /HDMI/HDMI_DETECT_B1
- R76 pad 1: +1.8V -> HDMI_5V0
- R76 pad 2: Net-(R76-Pad2) -> HDMI_SCL_B
- R77 pad 1: +1.8V -> HDMI_5V0
- R77 pad 2: Net-(R77-Pad2) -> HDMI_SDA_B
- R78 pad 1: +1.8V -> HDMI_DETECT
- R78 pad 2: Net-(R78-Pad2) -> GND
- R79 pad 1: ENCC0_Q0 -> +1.8V
- R79 pad 2: Net-(R75-Pad2) -> ENCC0_SW
- R80 pad 1: ENCC0_Q1 -> +1.8V
- R80 pad 2: Net-(R77-Pad2) -> ENCC2_SW
- R81 pad 1: ENCC2_Q0 -> +1.8V
- R81 pad 2: Net-(R76-Pad2) -> Net-(R81-Pad2)
- R82 pad 1: ENCC2_Q1 -> +1.8V
- R82 pad 2: Net-(R78-Pad2) -> Net-(R82-Pad2)
- R83 pad 2: ENCC1_SW -> Net-(R83-Pad2)
- R84 pad 1: +3V3 -> +1.8V
- R84 pad 2: ENCC3_SW -> Net-(R84-Pad2)
- R85 pad 1: +1.8V -> ENCC0_Q0
- R85 pad 2: Net-(R85-Pad2) -> Net-(R81-Pad2)
- R86 pad 1: +3V3 -> ENCC0_Q1
- R86 pad 2: Net-(R86-Pad2) -> Net-(R83-Pad2)
- R87 pad 1: +1.8V -> ENCC2_Q0
- R87 pad 2: Net-(R87-Pad2) -> Net-(R82-Pad2)
- R88 pad 1: +3V3 -> ENCC2_Q1
- R88 pad 2: Net-(R88-Pad2) -> Net-(R84-Pad2)
- R89 pad 1: ENCC1_Q0 -> +1.8V
- R89 pad 2: Net-(R85-Pad2) -> ENCC1_SW
- R90 pad 1: ENCC1_Q1 -> +3V3
- R90 pad 2: Net-(R87-Pad2) -> ENCC3_SW
- R91 pad 1: ENCC3_Q0 -> +1.8V
- R91 pad 2: Net-(R86-Pad2) -> Net-(R91-Pad2)
- R92 pad 1: ENCC3_Q1 -> +3V3
- R92 pad 2: Net-(R88-Pad2) -> Net-(R92-Pad2)
- R94 pad 1: +1.8V -> +3V3
- ROT1 pad A: Net-(R75-Pad2) -> Net-(R81-Pad2)
- ROT1 pad B: Net-(R77-Pad2) -> Net-(R83-Pad2)
- ROT2 pad A: Net-(R76-Pad2) -> Net-(R82-Pad2)
- ROT2 pad B: Net-(R78-Pad2) -> Net-(R84-Pad2)
- ROT3 pad A: Net-(R85-Pad2) -> Net-(R91-Pad2)
- ROT3 pad B: Net-(R87-Pad2) -> Net-(R93-Pad2)
- ROT4 pad A: Net-(R86-Pad2) -> Net-(R92-Pad2)
- ROT4 pad B: Net-(R88-Pad2) -> Net-(R94-Pad2)
- SW1 pad 3: TEMPO_SW -> /FPGA/GPIF II/TEMPO_LED_D
- U1 pad A10: (no net) -> RAM_LDM
- U1 pad A12: (no net) -> RAM_DQ2
- U1 pad A13: (no net) -> RAM_DQ7
- U1 pad A14: (no net) -> RAM_DQ6
- U1 pad A15: (no net) -> RAM_DQ10
- U1 pad A16: GND -> +1.8V
- U1 pad A8: (no net) -> RAM_UDQS_P
- U1 pad A9: (no net) -> RAM_UDQS_N
- U1 pad B10: (no net) -> RAM_DQ1
- U1 pad B11: (no net) -> RAM_DQ0
- U1 pad B12: (no net) -> RAM_DQ3
- U1 pad B13: GND -> +1.8V
- U1 pad B14: (no net) -> RAM_DQ8
- U1 pad B15: (no net) -> RAM_DQ11
- U1 pad B16: (no net) -> RAM_DQ12
- U1 pad B9: (no net) -> RAM_UDM
- U1 pad C10: GND -> +1.8V
- U1 pad C11: (no net) -> RAM_DQ15
- U1 pad C12: (no net) -> RAM_DQ14
- U1 pad C13: (no net) -> RAM_CK_N
- U1 pad C14: (no net) -> RAM_DQ9
- U1 pad C16: (no net) -> RAM_DQ13
- U1 pad C8: (no net) -> RAM_LDQS_P
- U1 pad C9: (no net) -> RAM_LDQS_N
- U1 pad D11: (no net) -> RAM_A2
- U1 pad D13: (no net) -> RAM_CK_P
- U1 pad D14: (no net) -> RAM_A5
- U1 pad D15: (no net) -> RAM_A4
- U1 pad D16: (no net) -> RAM_A8
- U1 pad D8: (no net) -> RAM_DQ5
- U1 pad D9: (no net) -> RAM_DQ4
- U1 pad E11: (no net) -> RAM_A3
- U1 pad E12: (no net) -> RAM_A1
- U1 pad E13: (no net) -> RAM_A0
- U1 pad E14: GND -> +1.8V
- U1 pad E15: (no net) -> RAM_A10
- U1 pad E16: (no net) -> RAM_A9
- U1 pad F12: (no net) -> RAM_A7
- U1 pad F13: (no net) -> RAM_A6
- U1 pad F14: (no net) -> RAM_CS#
- U1 pad F15: (no net) -> RAM_A11
- U1 pad G12: (no net) -> RAM_A12
- U1 pad G14: (no net) -> RAM_CKE
- U1 pad G15: (no net) -> RAM_RAS#
- U1 pad G16: (no net) -> RAM_CK_N
- U1 pad H12: (no net) -> RAM_BA1
- U1 pad H13: (no net) -> RAM_BA0
- U1 pad H15: GND -> +1.8V
- U1 pad H16: (no net) -> RAM_CK_P
- U1 pad J12: GND -> +1.8V
- U1 pad J15: (no net) -> RAM_CAS#
- U1 pad J16: (no net) -> RAM_WE#
- U3 pad 3: Net-(R93-Pad2) -> Net-(R44-Pad2)
- U3 pad 7: Net-(R94-Pad2) -> Net-(R45-Pad2)
- U9 pad 10: /SPIUSBBRIDGE/GPOUT6_BLUE_LED -> STATLED_BLUE
- U9 pad 9: /SPIUSBBRIDGE/GPOUT5_RED_LED -> STATLED_RED
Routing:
- net RAM_DQ12: track 0.00 -> 33.9 mm, vias 0 -> 2
- net RAM_CK_N: track 0.00 -> 23.8 mm, vias 0 -> 2
- net RAM_A0: track 0.00 -> 21.5 mm, vias 0 -> 1
- net RAM_A11: track 0.00 -> 20.8 mm, vias 0 -> 1
- net GA_0T: track 0.00 -> 20.3 mm, vias 0 -> 1
- net RAM_A10: track 0.00 -> 19.9 mm, vias 0 -> 1
- net RAM_DQ4: track 0.00 -> 19.5 mm, vias 0 -> 2
- net RAM_A3: track 0.00 -> 19.4 mm, vias 0 -> 1
- net RAM_DQ5: track 0.00 -> 19.0 mm, vias 0 -> 1
- net GPIF_SLCS#T: track 0.71 -> 19.6 mm
- net RAM_DQ9: track 0.00 -> 18.6 mm, vias 0 -> 2
- net RAM_A5: track 0.00 -> 18.6 mm, vias 0 -> 1
- net RAM_BA1: track 0.00 -> 18.6 mm, vias 0 -> 1
- net RAM_LDQS_N: track 0.00 -> 18.5 mm, vias 0 -> 1
- net RAM_A12: track 0.00 -> 18.5 mm, vias 0 -> 1
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- added copper zone on 1.0V, net +1.0V
- added copper zone on 1.8V, net GND
- added copper zone on GND, net GND
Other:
- board outline added: 265 x 60 mm
- copper layers 8 -> 10
